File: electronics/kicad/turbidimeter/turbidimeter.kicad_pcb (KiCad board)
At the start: 2 copper layers, 87 parts, among them U1 74HC595, U10 TSL2571FN, U11 TSL2571FN, U12 TSL2571FN, U13 TSL2571FN, U14 TSL2571FN, U15 TSL2571FN, U16 TSL2571FN, U17 74HC595, U18 TSL2571FN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

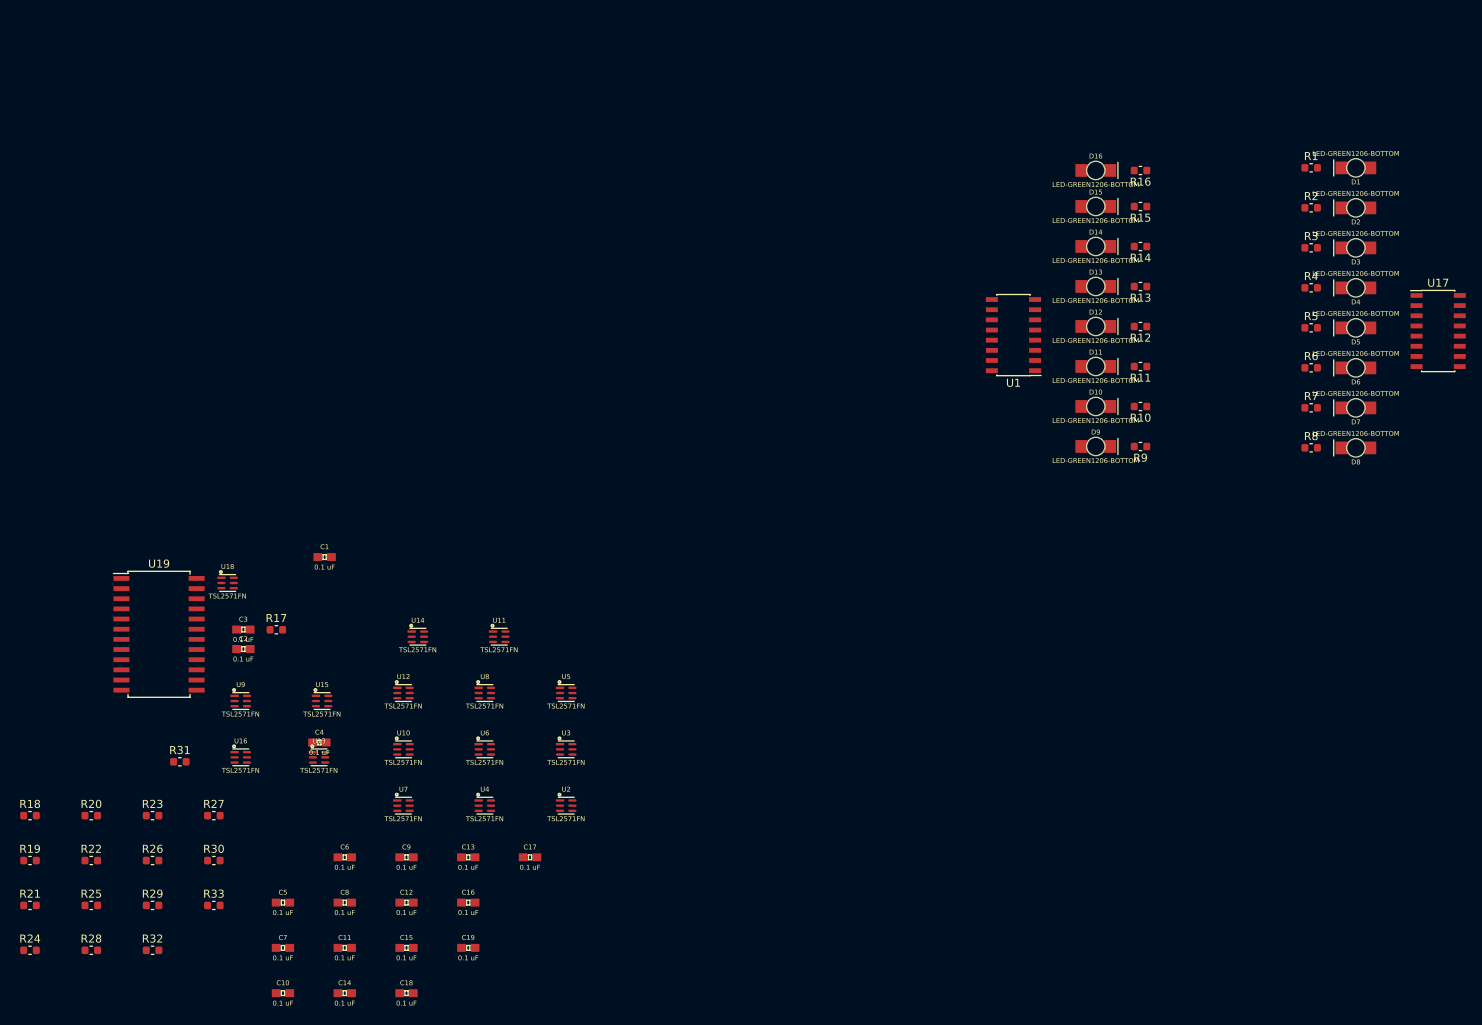
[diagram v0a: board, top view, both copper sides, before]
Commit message: Simple absorption/reflection calc
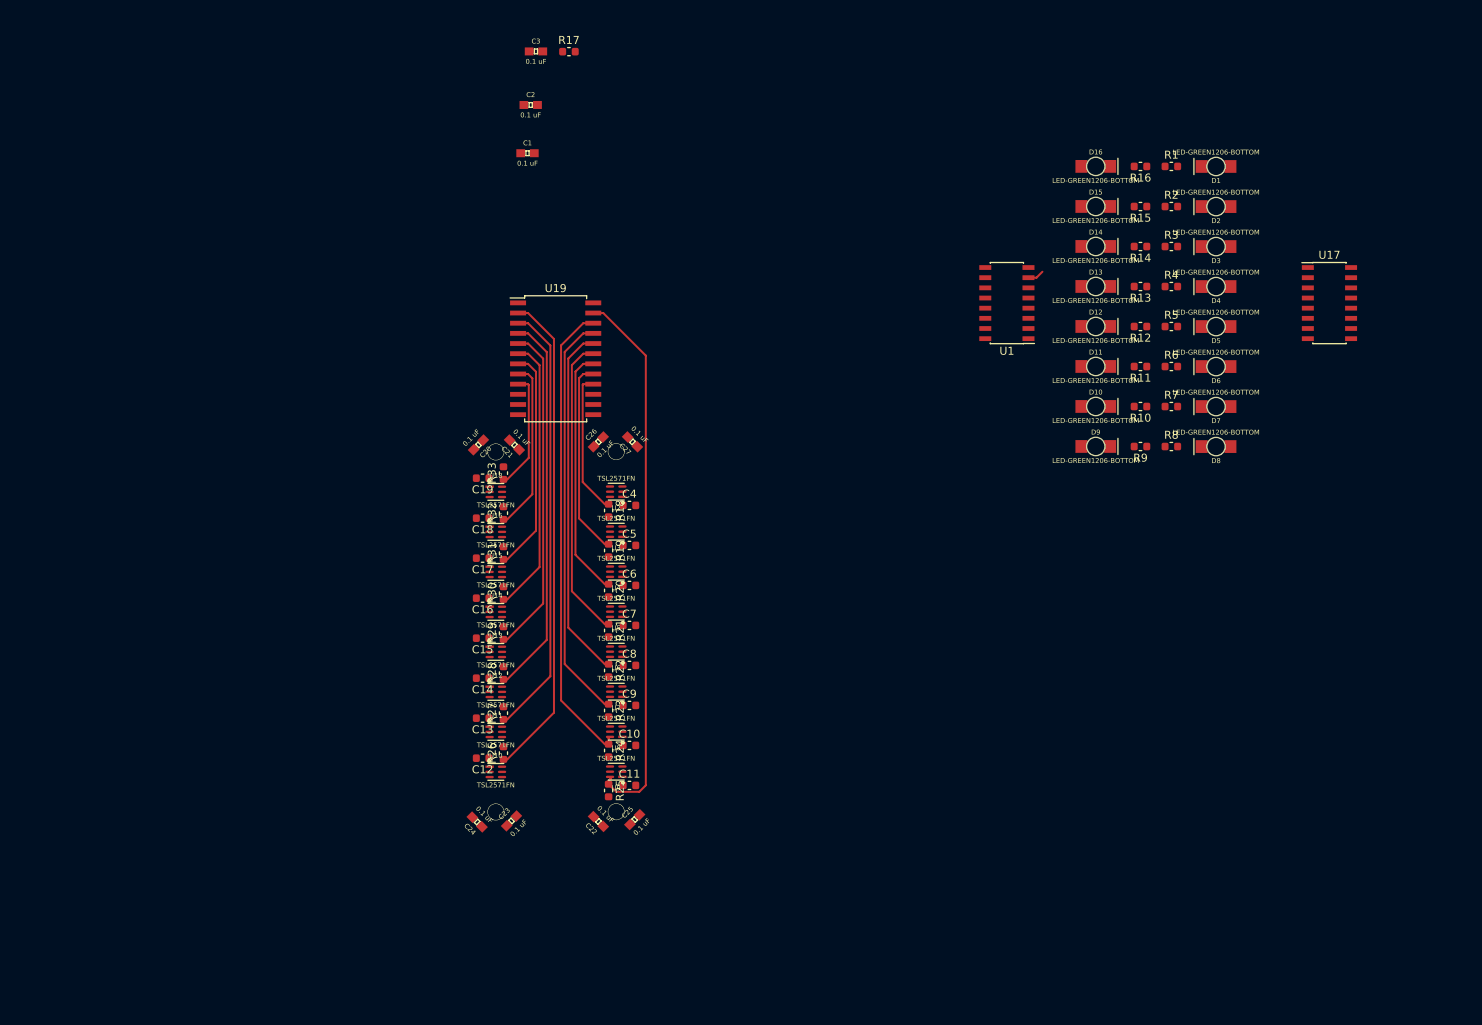
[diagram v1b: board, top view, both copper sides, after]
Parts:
- added C20: 0.1 uF, Capacitors:0603, F.Cu at (130.4, 72.1)
- added C21: 0.1 uF, Capacitors:0603, F.Cu at (134.8, 72.1)
- added C22: 0.1 uF, Capacitors:0603, F.Cu at (145.3, 119.2)
- added C23: 0.1 uF, Capacitors:0603, F.Cu at (134.5, 119.1)
- added C24: 0.1 uF, Capacitors:0603, F.Cu at (130.2, 119.2)
- added C25: 0.1 uF, Capacitors:0603, F.Cu at (149.9, 118.9)
- added C26: 0.1 uF, Capacitors:0603, F.Cu at (145.3, 71.7)
- added C27: 0.1 uF, Capacitors:0603, F.Cu at (149.6, 71.7)
- C10, C11, C12, C13, C14, C15, C16, C17, C18, C19, C4, C5, C6, C7, C8, C9: footprint Capacitors:0603 -> Capacitor_SMD:C_0603_1608Metric
- moved R19 82.1 mm to (146.6, 85.3), turned to 270 degrees
- moved R18 81.8 mm to (146.6, 80.3), turned to 270 degrees
- moved R17 81.0 mm to (141.7, 22.9)
- moved C3 81.0 mm to (137.5, 22.9)
- moved R21 80.1 mm to (146.6, 95.3), turned to 270 degrees
- moved C2 76.9 mm to (136.9, 29.6)
- moved R24 76.5 mm to (146.6, 110.3), turned to 270 degrees
- moved R20 70.5 mm to (146.6, 90.3), turned to 270 degrees
- moved R32 70.1 mm to (133.5, 80.6), turned to 90 degrees
- moved R22 68.9 mm to (146.6, 100.3), turned to 270 degrees
- moved R25 66.2 mm to (146.6, 115.3), turned to 270 degrees
- moved R33 65.0 mm to (133.5, 75.6), turned to 90 degrees
- moved C5 62.2 mm to (149.2, 84.6)
- moved R28 62.1 mm to (133.5, 100.6), turned to 90 degrees
- moved U19 60.4 mm to (140.0, 61.3)
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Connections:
- R17 pad 2: Net-(R17-Pad2) -> CLR
- R18 pad 1: /Sheet5FC47653/SDA_ -> /S15
- R19 pad 1: /sheet5FC57719/SDA_ -> /S14
- R20 pad 1: /sheet5FC5896F/SDA_ -> /S13
- R21 pad 1: /sheet5FC59297/SDA_ -> /S12
- R22 pad 1: /sheet5FC5B146/SDA_ -> /S11
- R23 pad 1: /sheet5FC5B147/SDA_ -> /S10
- R24 pad 1: /sheet5FC5B148/SDA_ -> /S9
- R25 pad 1: /sheet5FC5B149/SDA_ -> /S8
- R26 pad 1: /sheet5FC5BFF0/SDA_ -> /S7
- R27 pad 1: /sheet5FC5BFF1/SDA_ -> /S6
- R28 pad 1: /sheet5FC5BFF2/SDA_ -> /S5
- R29 pad 1: /sheet5FC5BFF3/SDA_ -> /S4
- R30 pad 1: /sheet5FC5BFF4/SDA_ -> /S3
- R31 pad 1: /sheet5FC5BFF5/SDA_ -> /S2
- R32 pad 1: /sheet5FC5BFF6/SDA_ -> /S1
- R33 pad 1: /sheet5FC5BFF7/SDA_ -> /S0
- U1 pad 10: Net-(U1-Pad10) -> CLR
- U1 pad 11: Net-(U1-Pad11) -> CLK
- U10 pad 6: /sheet5FC5BFF0/SDA_ -> /S7
- U11 pad 6: /sheet5FC5BFF1/SDA_ -> /S6
- U12 pad 6: /sheet5FC5BFF2/SDA_ -> /S5
- U13 pad 6: /sheet5FC5BFF3/SDA_ -> /S4
- U14 pad 6: /sheet5FC5BFF4/SDA_ -> /S3
- U15 pad 6: /sheet5FC5BFF5/SDA_ -> /S2
- U16 pad 6: /sheet5FC5BFF6/SDA_ -> /S1
- U17 pad 10: Net-(R17-Pad2) -> CLR
- U17 pad 11: Net-(U17-Pad11) -> CLK
- U18 pad 6: /sheet5FC5BFF7/SDA_ -> /S0
- U19 pad 16: Net-(U19-Pad16) -> /S15
- U19 pad 17: Net-(U19-Pad17) -> /S14
- U19 pad 18: Net-(U19-Pad18) -> /S13
- U19 pad 19: Net-(U19-Pad19) -> /S12
- U19 pad 2: Net-(U19-Pad2) -> /S7
- U19 pad 20: Net-(U19-Pad20) -> /S11
- U19 pad 21: Net-(U19-Pad21) -> /S10
- U19 pad 22: Net-(U19-Pad22) -> /S9
- U19 pad 23: Net-(U19-Pad23) -> /S8
- U19 pad 3: Net-(U19-Pad3) -> /S6
- U19 pad 4: Net-(U19-Pad4) -> /S5
- U19 pad 5: Net-(U19-Pad5) -> /S4
- U19 pad 6: Net-(U19-Pad6) -> /S3
- U19 pad 7: Net-(U19-Pad7) -> /S2
- U19 pad 8: Net-(U19-Pad8) -> /S1
- U19 pad 9: Net-(U19-Pad9) -> /S0
- U2 pad 6: /Sheet5FC47653/SDA_ -> /S15
- U3 pad 6: /sheet5FC57719/SDA_ -> /S14
- U4 pad 6: /sheet5FC5896F/SDA_ -> /S13
- U5 pad 6: /sheet5FC59297/SDA_ -> /S12
- U6 pad 6: /sheet5FC5B146/SDA_ -> /S11
- U7 pad 6: /sheet5FC5B147/SDA_ -> /S10
- U8 pad 6: /sheet5FC5B148/SDA_ -> /S9
- U9 pad 6: /sheet5FC5B149/SDA_ -> /S8
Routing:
- net /S8: track 0.00 -> 68.9 mm
- net /S7: track 0.00 -> 61.3 mm
- net /S9: track 0.00 -> 58.7 mm
- net /S6: track 0.00 -> 54.6 mm
- net /S10: track 0.00 -> 51.1 mm
- net /S5: track 0.00 -> 48.0 mm
- net /S11: track 0.00 -> 44.5 mm
- net /S4: track 0.00 -> 41.3 mm
- net /S12: track 0.00 -> 37.8 mm
- net /S3: track 0.00 -> 34.7 mm
- net /S13: track 0.00 -> 31.2 mm
- net /S2: track 0.00 -> 28.1 mm
- net /S14: track 0.00 -> 25.0 mm
- net /S1: track 0.00 -> 21.4 mm
- net /S15: track 0.00 -> 17.9 mm
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
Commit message: turbidimeter
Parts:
- removed C11: 0.1 uF, Capacitor_SMD:C_0603_1608Metric
- removed C20, C21, C22, C23, C24, C25, C26, C27: 0.1 uF, Capacitors:0603
- removed D10, D11, D12, D13, D14, D15, D16, D9: LED-GREEN1206-BOTTOM, LED:LED-1206-BOTTOM
- removed R11, R13, R15, R9: 330, Resistor_SMD:R_0603_1608Metric
- removed R18, R20, R22, R24: 10k, Resistor_SMD:R_0603_1608Metric
- removed U1: 74HC595, Package_SO:SOIC-16_3.9x9.9mm_P1.27mm
- removed U2, U3, U4, U5, U6, U7, U8, U9: TSL2571FN, Silicon-Standard:DFN-6-2X2
- added P1: CONN_6, Connectors2:1X06-SMD-FEMALE, F.Cu at (213.0, 26.7)
- added P2: CONN_6, Connectors2:1X06-SMD-FEMALE, F.Cu at (135.1, 91.0)
- added P3: CONN_6, Connectors2:1X06-SMD-FEMALE, F.Cu at (134.7, 56.1)
- added R34: 1, Capacitors:0805, F.Cu at (112.4, 51.6)
- added R35: 1, Capacitors:0805, F.Cu at (112.4, 63.6)
- added R36: 1, Capacitors:0805, F.Cu at (112.4, 69.6)
- added R37: 1, Capacitors:0805, F.Cu at (112.4, 75.6)
- added R38: 1, Capacitors:0805, F.Cu at (112.4, 81.6)
- added R39: 1, Capacitors:0805, F.Cu at (112.4, 87.6)
- added R40: 1, Capacitors:0805, F.Cu at (112.4, 93.6)
- added R41: 1, Capacitors:0805, F.Cu at (112.4, 57.6)
- added R42: 1, Capacitors:0805, F.Cu at (109.3, 53.5)
- added R43: 1, Capacitors:0805, F.Cu at (109.3, 65.5)
- added R44: 1, Capacitors:0805, F.Cu at (109.3, 71.5)
- added R45: 1, Capacitors:0805, F.Cu at (109.3, 77.5)
- added R46: 1, Capacitors:0805, F.Cu at (109.3, 83.5)
- added R47: 1, Capacitors:0805, F.Cu at (109.3, 89.5)
- added R48: 1, Capacitors:0805, F.Cu at (109.3, 95.5)
- added R49: 1, Capacitors:0805, F.Cu at (109.3, 59.5)
- C3: footprint Capacitors:0603 -> Capacitor_SMD:C_0603_1608Metric
- R10, R12, R14, R16: value 330 -> 1; footprint Resistor_SMD:R_0603_1608Metric -> Capacitors:0805
- R19, R21, R23, R25: value 10k -> 1; footprint Resistor_SMD:R_0603_1608Metric -> Capacitors:0805
- moved R16 108.4 mm to (112.5, 77.5), turned to 0 degrees
- moved R14 103.5 mm to (112.5, 71.5), turned to 0 degrees
- moved R10 101.6 mm to (112.5, 53.5), turned to 0 degrees
- moved R12 101.0 mm to (112.5, 65.5), turned to 0 degrees
- moved C2 81.9 mm to (215.4, 52.8), turned to 270 degrees
- moved R17 78.1 mm to (219.5, 30.0), turned to 270 degrees
- moved R25 65.4 mm to (112.5, 59.5), turned to 0 degrees
- moved U10 62.1 mm to (118.6, 52.4)
- moved R26 61.9 mm to (118.6, 50.6), turned to 180 degrees
- moved C12 61.0 mm to (114.8, 52.4), turned to 270 degrees
- moved C10 57.8 mm to (122.6, 58.4), turned to 90 degrees
- moved R27 51.6 mm to (118.5, 56.2), turned to 180 degrees
- moved U11 51.5 mm to (118.6, 58.4)
- moved C13 50.5 mm to (114.8, 58.4), turned to 270 degrees
- moved R8 45.9 mm to (229.9, 28.2), turned to 180 degrees
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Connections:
- C10 pad 1: 3.3V -> Net-(C10-Pad1)
- C10 pad 2: GND -> Net-(C10-Pad2)
- C12 pad 1: 3.3V -> Net-(C12-Pad1)
- C13 pad 1: 3.3V -> Net-(C13-Pad1)
- C14 pad 1: 3.3V -> Net-(C14-Pad1)
- C15 pad 1: 3.3V -> Net-(C15-Pad1)
- C16 pad 1: 3.3V -> Net-(C16-Pad1)
- C17 pad 1: 3.3V -> Net-(C17-Pad1)
- C18 pad 1: 3.3V -> Net-(C18-Pad1)
- C19 pad 1: 3.3V -> Net-(C19-Pad1)
- C3 pad 1: 3.3V -> Net-(C3-Pad1)
- C3 pad 2: GND -> Net-(C3-Pad2)
- C4 pad 1: 3.3V -> Net-(C4-Pad1)
- C4 pad 2: GND -> Net-(C4-Pad2)
- C5 pad 1: 3.3V -> Net-(C5-Pad1)
- C5 pad 2: GND -> Net-(C5-Pad2)
- C6 pad 1: 3.3V -> Net-(C6-Pad1)
- C6 pad 2: GND -> Net-(C6-Pad2)
- C7 pad 1: 3.3V -> Net-(C7-Pad1)
- C7 pad 2: GND -> Net-(C7-Pad2)
- C8 pad 1: 3.3V -> Net-(C8-Pad1)
- C8 pad 2: GND -> Net-(C8-Pad2)
- C9 pad 1: 3.3V -> Net-(C9-Pad1)
- C9 pad 2: GND -> Net-(C9-Pad2)
- R10 pad 1: GND -> Net-(R10-Pad1)
- R10 pad 2: Net-(D10-PadC) -> Net-(R10-Pad2)
- R12 pad 1: GND -> Net-(R12-Pad1)
- R12 pad 2: Net-(D12-PadC) -> Net-(R12-Pad2)
- R14 pad 1: GND -> Net-(R14-Pad1)
- R14 pad 2: Net-(D14-PadC) -> Net-(R14-Pad2)
- R16 pad 1: GND -> Net-(R16-Pad1)
- R16 pad 2: Net-(D16-PadC) -> Net-(R16-Pad2)
- R19 pad 1: /S14 -> Net-(R19-Pad1)
- R19 pad 2: 3.3V -> Net-(R19-Pad2)
- R21 pad 1: /S12 -> Net-(R21-Pad1)
- R21 pad 2: 3.3V -> Net-(R21-Pad2)
- R23 pad 1: /S10 -> Net-(R23-Pad1)
- R23 pad 2: 3.3V -> Net-(R23-Pad2)
- R25 pad 1: /S8 -> Net-(R25-Pad1)
- R25 pad 2: 3.3V -> Net-(R25-Pad2)
- R26 pad 2: 3.3V -> Net-(C12-Pad1)
- R27 pad 2: 3.3V -> Net-(C13-Pad1)
- R28 pad 2: 3.3V -> Net-(C14-Pad1)
- R29 pad 2: 3.3V -> Net-(C15-Pad1)
- R30 pad 2: 3.3V -> Net-(C16-Pad1)
- R31 pad 2: 3.3V -> Net-(C17-Pad1)
- R32 pad 2: 3.3V -> Net-(C18-Pad1)
- R33 pad 2: 3.3V -> Net-(C19-Pad1)
- U10 pad 1: 3.3V -> Net-(C12-Pad1)
- U10 pad 2: SCL -> Net-(R10-Pad2)
- U11 pad 1: 3.3V -> Net-(C13-Pad1)
- U11 pad 2: SCL -> Net-(R25-Pad2)
- U12 pad 1: 3.3V -> Net-(C14-Pad1)
- U12 pad 2: SCL -> Net-(R12-Pad2)
- U13 pad 1: 3.3V -> Net-(C15-Pad1)
- U13 pad 2: SCL -> Net-(R14-Pad2)
- U14 pad 1: 3.3V -> Net-(C16-Pad1)
- U14 pad 2: SCL -> Net-(R16-Pad2)
- U15 pad 1: 3.3V -> Net-(C17-Pad1)
- U15 pad 2: SCL -> Net-(R19-Pad2)
- U16 pad 1: 3.3V -> Net-(C18-Pad1)
- U16 pad 2: SCL -> Net-(R21-Pad2)
- U17 pad 14: Net-(U17-Pad14) -> SER
- U18 pad 1: 3.3V -> Net-(C19-Pad1)
- U18 pad 2: SCL -> Net-(R23-Pad2)
- U19 pad 1: Net-(U19-Pad1) -> SDA
- U19 pad 10: Net-(U19-Pad10) -> A1
- U19 pad 11: Net-(U19-Pad11) -> A0
- U19 pad 13: Net-(U19-Pad13) -> A3
- U19 pad 14: Net-(U19-Pad14) -> A2
- U19 pad 15: Net-(U19-Pad15) -> GND
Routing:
- net 3.3V: track 0.00 -> 136.4 mm
- net GND: track 0.00 -> 103.4 mm, vias 0 -> 2
- net SCL: track 0.00 -> 69.3 mm
- net /S8: track 68.9 -> 0.00 mm
- net /S9: track 58.7 -> 0.00 mm
- net /S10: track 51.1 -> 0.00 mm
- net /S11: track 44.5 -> 0.00 mm
- net /S7: track 61.3 -> 21.4 mm
- net /S12: track 37.8 -> 0.00 mm
- net /S6: track 54.6 -> 17.1 mm
- net /S5: track 48.0 -> 12.0 mm
- net /S4: track 41.3 -> 9.91 mm
- net /S13: track 31.2 -> 0.00 mm
- net SDA: track 0.00 -> 27.1 mm
- net SER: track 0.00 -> 26.9 mm
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- added copper zone on F.Cu, net GND

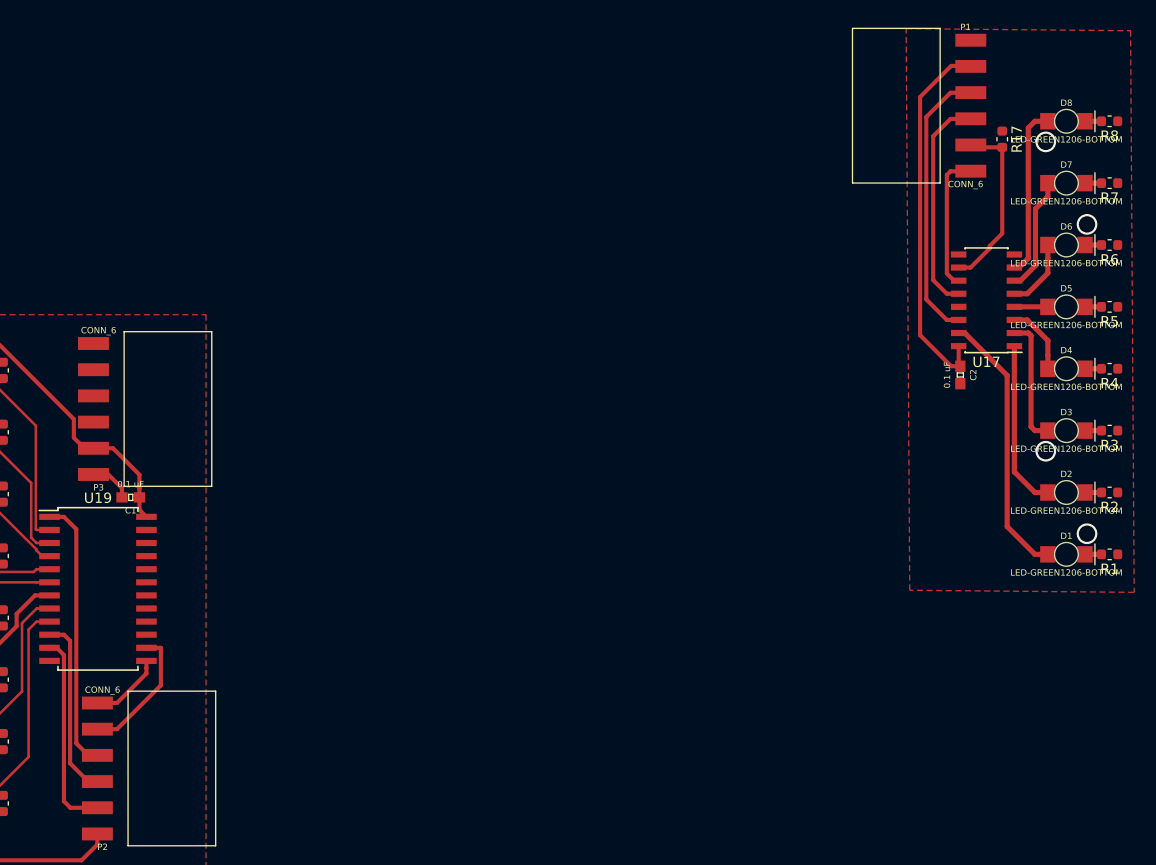
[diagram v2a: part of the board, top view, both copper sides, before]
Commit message: Cuvette; access hole is too large, film might not seal
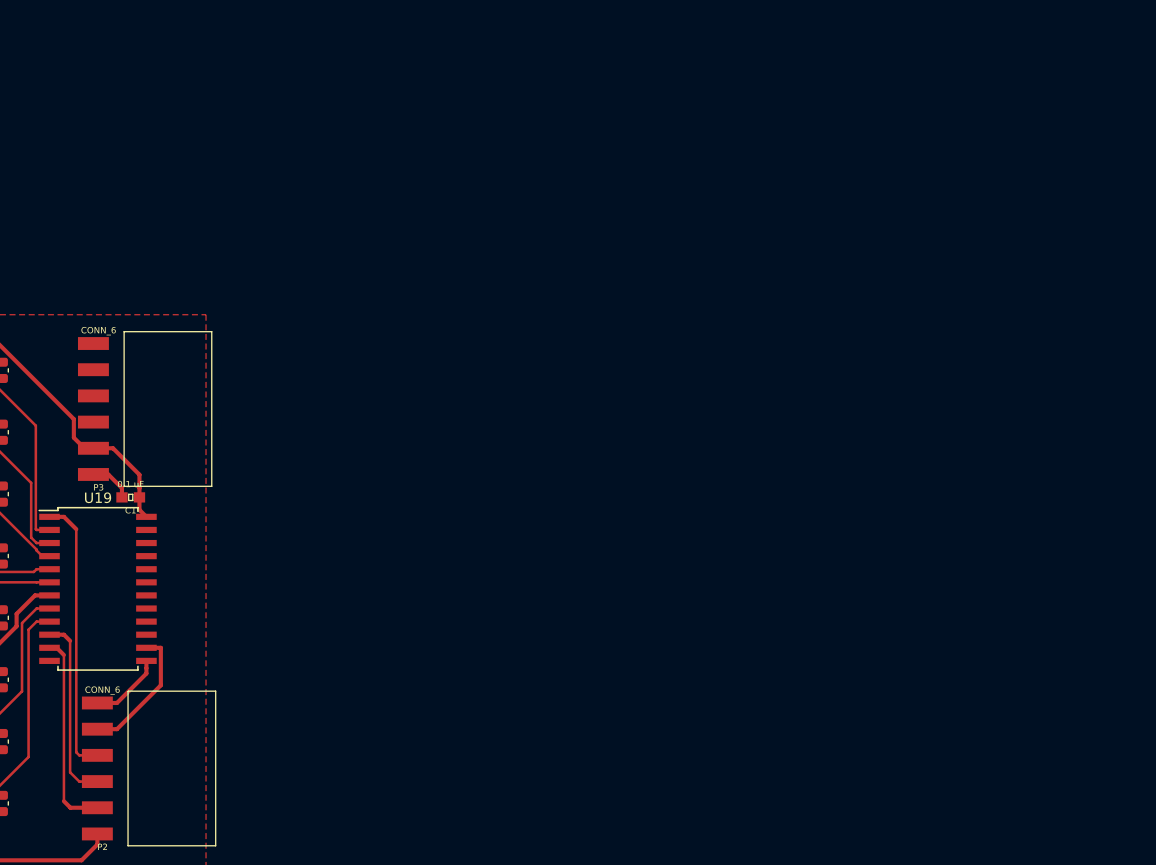
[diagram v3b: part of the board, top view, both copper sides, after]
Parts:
- removed C2: 0.1 uF, Capacitors:0603
- removed D1, D2, D3, D4, D5, D6, D7, D8: LED-GREEN1206-BOTTOM, LED:LED-1206-BOTTOM
- removed P1: CONN_6, Connectors2:1X06-SMD-FEMALE
- removed R1, R2, R3, R4, R5, R6, R7, R8: 330, Resistor_SMD:R_0603_1608Metric
- removed R17: 1k, Resistor_SMD:R_0603_1608Metric
- removed U17: 74HC595, Package_SO:SOIC-16_3.9x9.9mm_P1.27mm
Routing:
- net 3.3V: track 136.4 -> 100.0 mm
- net SER: track 26.9 -> 0.00 mm
- net /Sheet5FC1C284/SEL: track 26.1 -> 0.00 mm
- net LATCH: track 22.1 -> 0.00 mm
- net CLR: track 18.2 -> 0.00 mm
- net /sheet5FC22DDC/SEL: track 16.5 -> 0.00 mm
- net /sheet5FC224EF/SEL: track 16.3 -> 0.00 mm
- net CLK: track 13.4 -> 0.00 mm
- net /sheet5FC225C3/SEL: track 12.3 -> 0.00 mm
- net /sheet5FC22DDB/SEL: track 11.1 -> 0.00 mm
- net /sheet5FC22669/SEL: track 6.81 -> 0.00 mm
- net /sheet5FC22DDA/SEL: track 6.80 -> 0.00 mm
- net /sheet5FC227E0/SEL: track 3.25 -> 0.00 mm
- net Net-(D8-PadC): track 1.61 -> 0.00 mm
- net Net-(D7-PadC): track 1.61 -> 0.00 mm
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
